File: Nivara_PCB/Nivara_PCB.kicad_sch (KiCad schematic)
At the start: 27 parts, among them J11 PINHD_1x2_Female, U18 RS485, U19 ANALOG_OUT., U20 ANALOG_IN, U21 RELAY, U22 NPN_IN, U23 PNP_IN, U24 D_IN, U25 RUN/STOP, U26 NPN_OUT, U27 PNP_OUT, U28 FUENTE IN, U29 FUENTE EX, U30 GT-USB-7010ASV

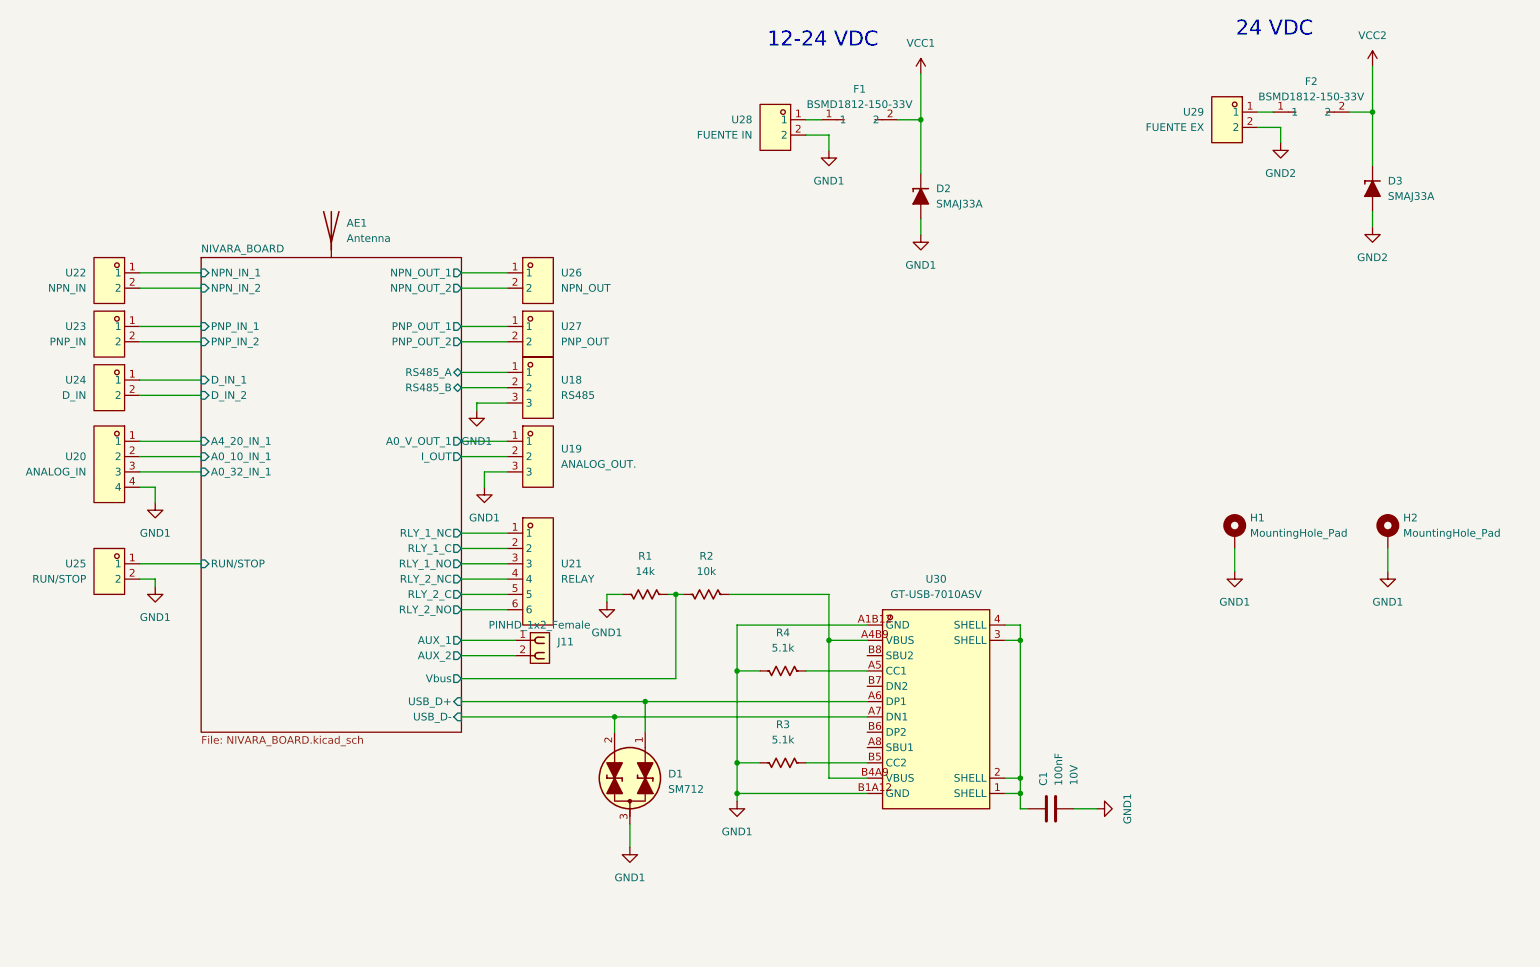
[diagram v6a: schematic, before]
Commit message: Cambios realizados en el PCB y el esquema de Nivara_PCB.
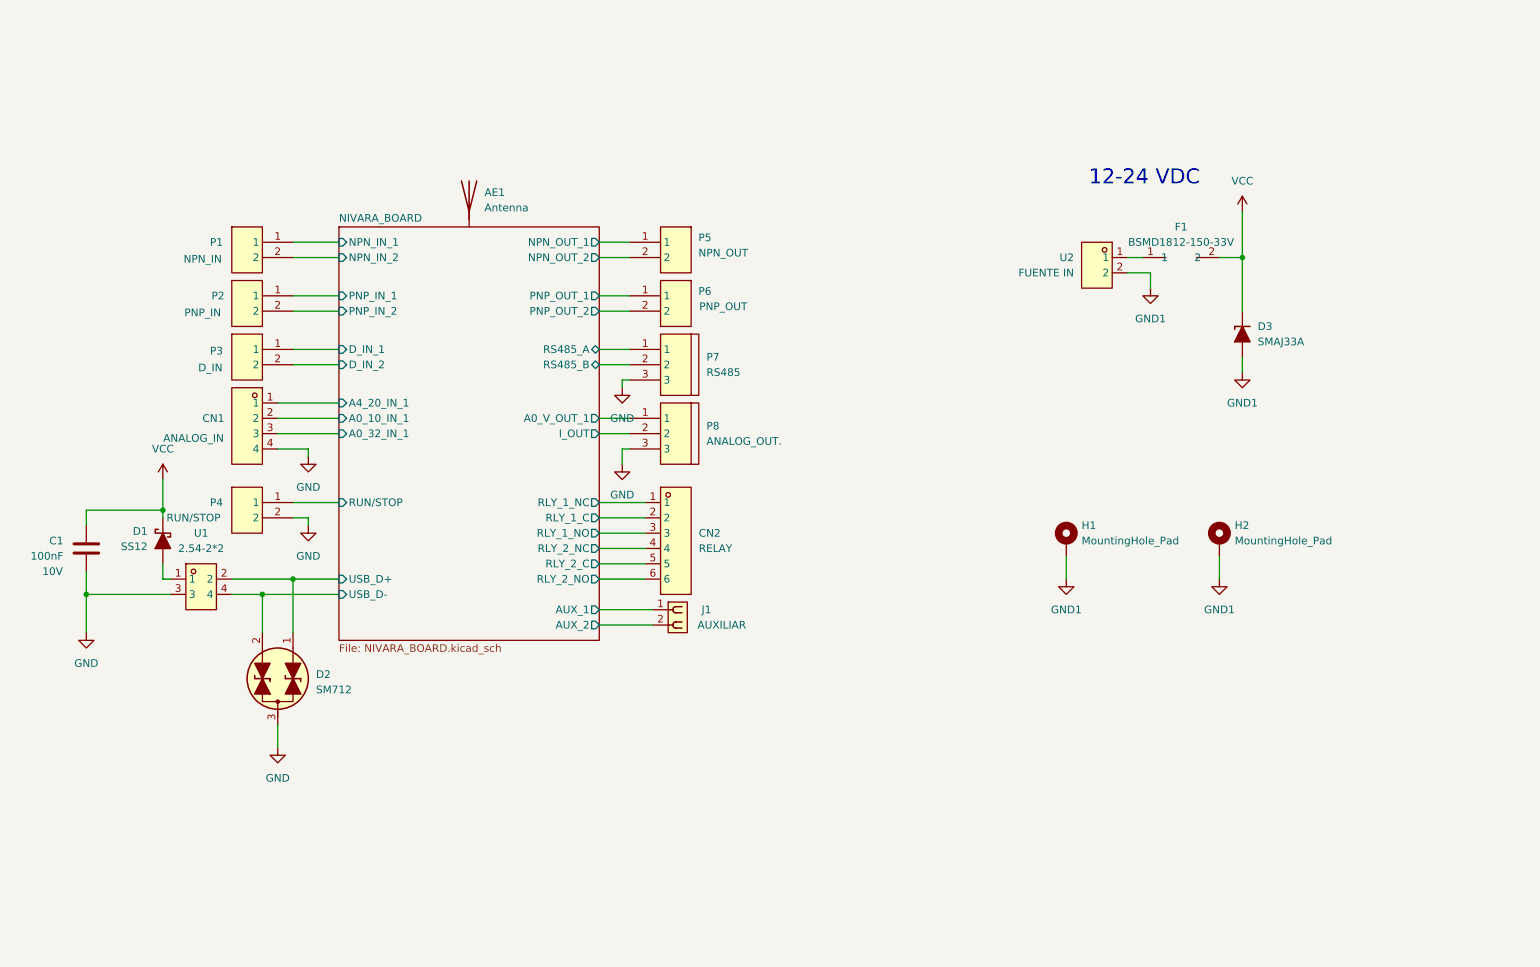
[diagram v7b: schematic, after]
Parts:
- removed D1: SM712, PCM_Package_TO_SOT_SMD_AKL:SOT-23, symbol PCM_Diode_TVS_AKL:SM712
- removed D3: SMAJ33A, PCM_Diode_SMD_AKL:D_SMA, symbol PCM_Diode_TVS_AKL:SMAJ33A
- removed F2: BSMD1812-150-33V, EasyEDA:F1812, symbol EasyEDA:BSMD1812-150-33V
- removed R1: 14k, PCM_Resistor_SMD_AKL:R_0603_1608Metric, symbol PCM_Resistor_US_AKL:R_0603
- removed R2: 10k, PCM_Resistor_SMD_AKL:R_0603_1608Metric, symbol PCM_Resistor_US_AKL:R_0603
- removed R3, R4: 5.1k, PCM_Resistor_SMD_AKL:R_0805_2012Metric, symbol PCM_Resistor_US_AKL:R_0805
- removed U18: RS485, EasyEDA:CONN-TH_XY126V-5.0-3P, symbol EasyEDA:XY126V-5.0-3P
- removed U19: ANALOG_OUT., EasyEDA:CONN-TH_XY126V-5.0-3P, symbol EasyEDA:XY126V-5.0-3P
- removed U20: ANALOG_IN, EasyEDA:CONN-TH_4P-P5.00_DIBO_DB126V-5.0-4P-GN-P, symbol EasyEDA:DB126V-5.0-4P-GN-P
- removed U21: RELAY, EasyEDA:CONN-TH_DB126V-5.0-6P-GN, symbol EasyEDA:DB126V-5.0-6P-GN
- removed U22: NPN_IN, EasyEDA:CONN-TH_XY126V-5.0-2P, symbol EasyEDA:XY126V-5.0-2P
- removed U23: PNP_IN, EasyEDA:CONN-TH_XY126V-5.0-2P, symbol EasyEDA:XY126V-5.0-2P
- removed U24: D_IN, EasyEDA:CONN-TH_XY126V-5.0-2P, symbol EasyEDA:XY126V-5.0-2P
- removed U25: RUN/STOP, EasyEDA:CONN-TH_XY126V-5.0-2P, symbol EasyEDA:XY126V-5.0-2P
- removed U26: NPN_OUT, EasyEDA:CONN-TH_XY126V-5.0-2P, symbol EasyEDA:XY126V-5.0-2P
- removed U27: PNP_OUT, EasyEDA:CONN-TH_XY126V-5.0-2P, symbol EasyEDA:XY126V-5.0-2P
- removed U29: FUENTE EX, EasyEDA:CONN-TH_XY126V-5.0-2P, symbol EasyEDA:XY126V-5.0-2P
- removed U30: GT-USB-7010ASV, EasyEDA:USB-C-SMD_G-SWITCH_GT-USB-7010ASV, symbol EasyEDA:GT-USB-7010ASV
- added CN1: ANALOG_IN, EasyEDA:CONN-TH_DB128V-5.0-4P, symbol EasyEDA:DB128V-5.08-4P-GN-S
- added CN2: RELAY, EasyEDA:CONN-TH_DB126V-5.0-6P-GN, symbol EasyEDA:DB128V-5.08-6P-GN-S
- added D1: SS12, PCM_Diode_SMD_AKL:D_SMA, symbol PCM_Diode_Schottky_AKL:SS12
- added D2: SM712, PCM_Package_TO_SOT_SMD_AKL:SOT-23, symbol PCM_Diode_TVS_AKL:SM712
- added P1: NPN_IN, EasyEDA:CONN-TH_XY126V-5.0-2P, symbol EasyEDA:WJ500V-5.08-2P-14-00A
- added P2: PNP_IN, EasyEDA:CONN-TH_XY126V-5.0-2P, symbol EasyEDA:WJ500V-5.08-2P-14-00A
- added P3: D_IN, EasyEDA:CONN-TH_XY126V-5.0-2P, symbol EasyEDA:WJ500V-5.08-2P-14-00A
- added P4: RUN/STOP, EasyEDA:CONN-TH_XY126V-5.0-2P, symbol EasyEDA:WJ500V-5.08-2P-14-00A
- added P5: NPN_OUT, EasyEDA:CONN-TH_XY126V-5.0-2P, symbol EasyEDA:WJ500V-5.08-2P-14-00A
- added P6: PNP_OUT, EasyEDA:CONN-TH_XY126V-5.0-2P, symbol EasyEDA:WJ500V-5.08-2P-14-00A
- added P7: RS485, EasyEDA:CONN-TH_3P-P5.00_WJ500V-5.08-3P, symbol EasyEDA:WJ500V-5.08-3P-14-00A
- added P8: ANALOG_OUT., EasyEDA:CONN-TH_3P-P5.00_WJ500V-5.08-3P, symbol EasyEDA:WJ500V-5.08-3P-14-00A
- added U1: 2.54-2*2, Connector_PinHeader_2.54mm:PinHeader_2x02_P2.54mm_Vertical, symbol EasyEDA:2.54-2*2
- J1: renamed from J11; value PINHD_1x2_Female -> AUXILIAR
- renumbered D2 to D3, U28 to U2
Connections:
- net VCC1 is gone; now on net VCC: D3.1 (K), F1.2
- net GND1: no longer C1.2
- net NIVARA_BOARD/A0_10_IN_1: now also CN1.2
- net NIVARA_BOARD/A0_32_IN_1: now also CN1.3
- net NIVARA_BOARD/A0_V_OUT_1: now also P8.1
- net NIVARA_BOARD/A4_20_IN_1: now also CN1.1
- net NIVARA_BOARD/D_IN_1: now also P3.1
- net NIVARA_BOARD/D_IN_2: now also P3.2
- net NIVARA_BOARD/I_OUT: now also P8.2
- net NIVARA_BOARD/NPN_IN_1: now also P1.1
- net NIVARA_BOARD/NPN_IN_2: now also P1.2
- net NIVARA_BOARD/NPN_OUT_1: now also P5.1
- net NIVARA_BOARD/NPN_OUT_2: now also P5.2
- net NIVARA_BOARD/PNP_IN_1: now also P2.1
- net NIVARA_BOARD/PNP_IN_2: now also P2.2
- net NIVARA_BOARD/PNP_OUT_1: now also P6.1
- net NIVARA_BOARD/PNP_OUT_2: now also P6.2
- net NIVARA_BOARD/RLY_1_C: now also CN2.2
- net NIVARA_BOARD/RLY_1_NC: now also CN2.1
- net NIVARA_BOARD/RLY_1_NO: now also CN2.3
- net NIVARA_BOARD/RLY_2_C: now also CN2.5
- net NIVARA_BOARD/RLY_2_NC: now also CN2.4
- net NIVARA_BOARD/RLY_2_NO: now also CN2.6
- net NIVARA_BOARD/RS485_A: now also P7.1
- net NIVARA_BOARD/RS485_B: now also P7.2
- net NIVARA_BOARD/RUN/STOP: now also P4.1
- net NIVARA_BOARD/USB_D+: now also D2.1 (A1), U1.2
- net NIVARA_BOARD/USB_D-: now also D2.2 (A2), U1.4
- net VCC: now reaches C1.1
- net VCC: now also D1.1 (K)
- new net: D1.2 (A), U1.1
- new net GND: C1.2, CN1.4, D2.3 (Com), P4.2, P7.3, P8.3, U1.3
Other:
- sheet NIVARA_BOARD ports: added none; removed Vbus
- note removed: "24 VDC"
- moved on the sheet: AE1, D3, F1, H1, H2, J1, U2

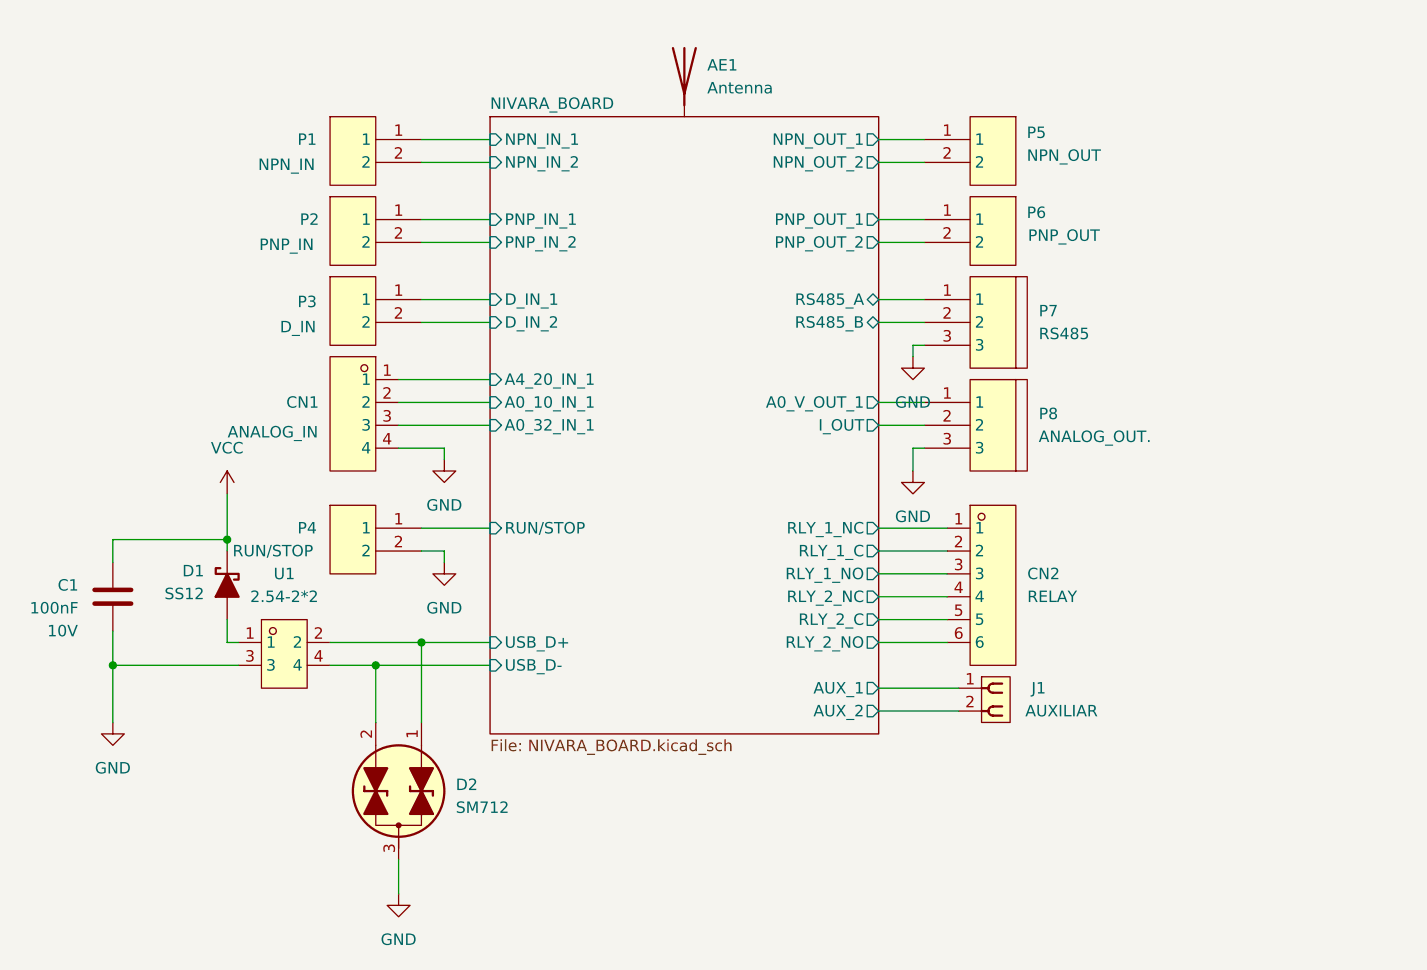
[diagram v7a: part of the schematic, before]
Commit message: Cambios realizados en los archivos de Nivara_PCB.
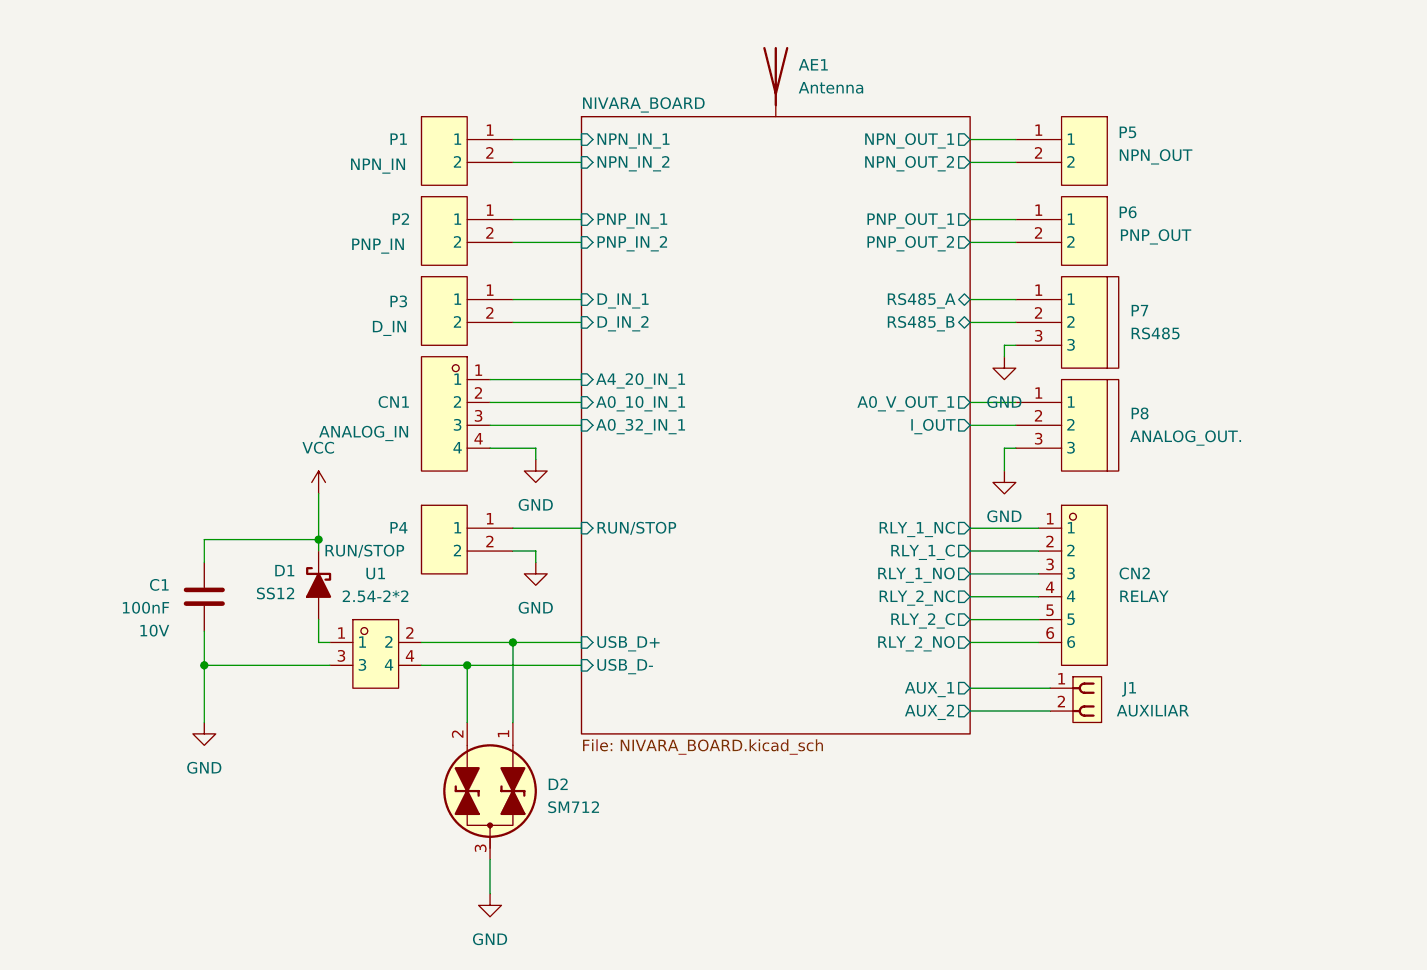
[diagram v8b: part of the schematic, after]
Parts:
- AE1: symbol Device:Antenna -> EasyEDA:Antenna
- C1: symbol PCM_Capacitor_US_AKL:C_0603 -> EasyEDA:C_0603
- D1: symbol PCM_Diode_Schottky_AKL:SS12 -> EasyEDA:SS12
- D2: symbol PCM_Diode_TVS_AKL:SM712 -> EasyEDA:SM712
- D3: symbol PCM_Diode_TVS_AKL:SMAJ33A -> EasyEDA:SMAJ33A
- H1, H2: symbol Mechanical:MountingHole_Pad -> EasyEDA:MountingHole_Pad
- J1: symbol PCM_SL_Pin_Headers:PINHD_1x2_Female -> EasyEDA:PINHD_1x2_Female
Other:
- moved on the sheet: AE1, C1, CN1, CN2, D1, D2, J1, P1, P2, P3, P4, P5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
